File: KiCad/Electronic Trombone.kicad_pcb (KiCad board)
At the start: 2 copper layers, 167 parts, among them J1 691137710004, J2 691137710003, J3 691137710003, J4 691137710002, Q1 NPN, Q2 PNP, Q3 NPN, Q4 PNP, Q5 NPN, Q6 NPN, SW1 SW_Push_Dual, SW2 SW_Push_Dual, SW3 SW_Push_Dual, SW4 SW_DPST, U1 CD74HC4051E, U10 TL074, U2 TL074, U3 TL074, U4 40106, U5 TL074, U6 TL074, U7 TL074, U8 TL074, U9 TL074

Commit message: started pcb layout
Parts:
- moved R17 217.5 mm to (-79.6, 83.8)
- moved C20 213.4 mm to (-189.7, 101.9)
- moved C21 213.4 mm to (-189.7, 103.6)
- moved C22 213.4 mm to (-189.7, 105.4)
- moved C23 213.4 mm to (-189.7, 107.1)
- moved C24 213.4 mm to (-189.7, 108.9)
- moved C25 213.4 mm to (-189.7, 110.6)
- moved C26 213.4 mm to (-189.7, 112.4)
- moved C27 213.4 mm to (-189.7, 114.1)
- moved C5 213.4 mm to (-180.4, 139.6)
- moved C6 213.4 mm to (-180.4, 146.2)
- moved C7 213.4 mm to (-180.4, 152.7)
- moved J4 213.4 mm to (-177.8, 105.3)
- moved R18 213.4 mm to (-73.3, 69.8)
- moved R20 213.4 mm to (-73.3, 71.6)
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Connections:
- net Net-(D1-K) renamed //Oscillator/Sch Inv In 1
- net Net-(D2-K) renamed //Oscillator/Sch Inv In 2
- net Net-(R17-Pad1) renamed //Oscillator/Tuning 1
- net Net-(R26-Pad1) renamed //Oscillator/Tuning 2
- net Net-(U1-S0) renamed //Trigger 1
- net Net-(U1-S1) renamed //Trigger 2
- net Net-(U1-S2) renamed //Trigger 3
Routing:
- net GND: track 0.00 -> 21.0 mm
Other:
- board outline added: 150 x 100 mm

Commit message: added osc core and tuning to pcb layout
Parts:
- R19, R28: value 2.5k -> 2.4k; footprint Resistor_SMD:R_0603_1608Metric -> Resistor_SMD:R_0201_0603Metric
- moved SW1 259.3 mm to (69.2, 113.5)
- moved J4 249.6 mm to (71.8, 103.0)
- moved SW2 247.3 mm to (69.2, 127.2)
- moved SW4 237.7 mm to (123.0, 82.5), turned to 90 degrees
- moved SW3 236.0 mm to (69.0, 141.0)
- moved TH4 199.6 mm to (101.9, 78.5), turned to 180 degrees
- moved TH6 199.3 mm to (101.9, 70.0), turned to 180 degrees
- moved TH5 199.2 mm to (101.9, 61.5), turned to 180 degrees
- moved RV10 193.2 mm to (130.0, 53.1), turned to 180 degrees
- moved R27 176.1 mm to (105.0, 83.2)
- moved R22 175.2 mm to (101.6, 84.1)
- moved R24 175.1 mm to (101.6, 85.0), turned to 180 degrees
- moved R23 175.1 mm to (101.6, 83.2)
- moved J3 166.7 mm to (54.5, 107.0), turned to -90 degrees
- moved R26 165.6 mm to (94.1, 56.7)
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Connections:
- J1 pad 1: //Pot Out -> //Audio Out
- J1 pad 2: //Audio Out -> //Pot Out
- R20 pad 2: Net-(U5C-+) -> Net-(U5D-+)
- R21 pad 2: Net-(U5C-+) -> Net-(U5D-+)
- SW4 pad 1: Net-(B2-Pad2) -> Net-(B1-Pad1)
- SW4 pad 2: -9V -> +9V
- SW4 pad 3: Net-(B1-Pad1) -> Net-(B2-Pad2)
- SW4 pad 4: +9V -> -9V
- U5 pad 1: //Oscillator/Mix In 1 -> //Oscillator/Mix In 2
- U5 pad 10: Net-(U5C-+) -> GND
- U5 pad 12: GND -> Net-(U5D-+)
- U5 pad 13: Net-(U5D--) -> //Filter/Signal In
- U5 pad 14: Net-(U5D--) -> //Filter/Signal In
- U5 pad 2: //Oscillator/Mix In 1 -> //Oscillator/Mix In 2
- U5 pad 3: //Oscillator/Sch Inv In 1 -> //Oscillator/Sch Inv In 2
- U5 pad 5: //Oscillator/Sch Inv In 2 -> //Oscillator/Sch Inv In 1
- U5 pad 6: //Oscillator/Mix In 2 -> //Oscillator/Mix In 1
- U5 pad 7: //Oscillator/Mix In 2 -> //Oscillator/Mix In 1
- U5 pad 8: //Filter/Signal In -> Net-(U5C--)
- U5 pad 9: //Filter/Signal In -> Net-(U5C--)
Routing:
- net GND: track 21.0 -> 0.00 mm
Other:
- board text added: "-Control Buttons Board Below-"
- board text added: "-Pot Terminals Control Board Below-"
- board text added: "Tr. 1"
- board text added: "Tr. 2"
- board text added: "Tr. 3"

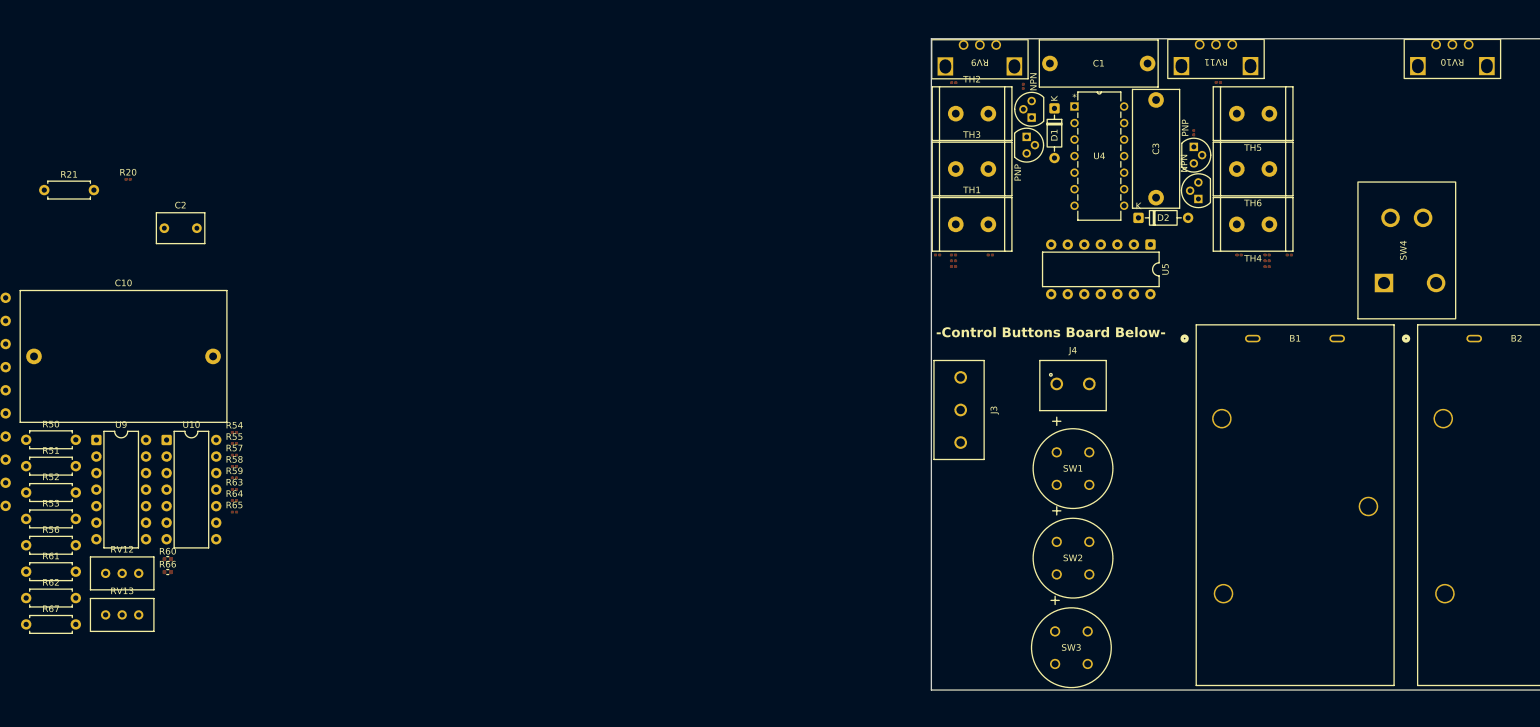
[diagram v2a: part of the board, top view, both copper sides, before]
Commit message: added osc output processing to pcb layout
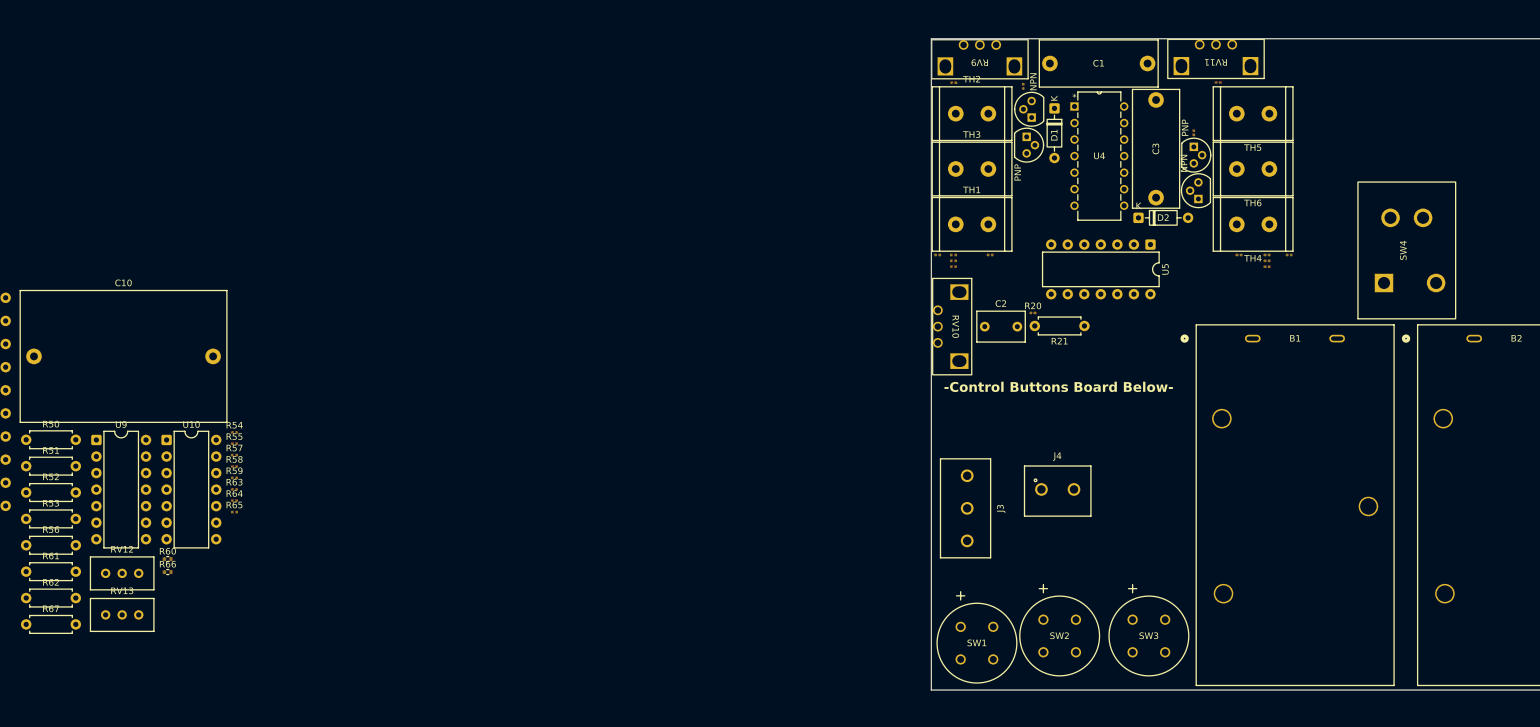
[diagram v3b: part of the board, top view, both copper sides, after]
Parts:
- moved R21 161.1 mm to (73.5, 94.1), turned to 180 degrees
- moved R20 140.4 mm to (65.6, 92.1)
- moved C2 126.9 mm to (58.2, 94.2)
- moved RV10 87.1 mm to (53.2, 94.2), turned to -90 degrees
- moved SW1 30.6 mm to (54.5, 140.3)
- moved J4 16.4 mm to (69.4, 119.2)
- moved J3 15.1 mm to (55.5, 122.1)
- moved SW2 12.1 mm to (67.2, 139.2)
- moved SW3 12.0 mm to (80.9, 139.2)
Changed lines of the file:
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@@
 	(footprint "Resistor_SMD:R_0201_0603Metric"
 		(layer "F.Cu")
-		(at -73.325 71.585)
+		(at 65.6 92.1)
 		(descr "Resistor SMD 0201 (0603 Metric), square (rectangular) end terminal, IPC-7351 nominal, (Body size source: https://www.vishay.com/docs/20052/crcw0201e3.pdf)")
 		(tags "resistor")
@@
 	(footprint "Header 691137710002:691137710002"
 		(layer "F.Cu")
-		(at 71.75 103)
+		(at 69.4 119.2)
 		(property "Reference" "J4"
 			(at 0 -5.135 0)
@@
 	(footprint "Switch Push Button D6R90F2LFS:D6R90_CNK"
 		(layer "F.Cu")
-		(at 69.25 127.25)
+		(at 67.2 139.2)
 		(tags "D6R90F2LFS ")
 		(property "Reference" "SW2"
@@
 	(footprint "Resistor_THT:R_Axial_DIN0207_L6.3mm_D2.5mm_P7.62mm_Horizontal"
 		(layer "F.Cu")
-		(at -86.205 73.235)
+		(at 73.5 94.1 180)
 		(descr "Resistor, Axial_DIN0207 series, Axial, Horizontal, pin pitch=7.62mm, 0.25W = 1/4W, length*diameter=6.3*2.5mm^2, http://cdn-reichelt.de/documents/datenblatt/B400/1_4W%23YAG.pdf")
 		(tags "Resistor Axial_DIN0207 series Axial Horizontal pin pitch 7.62mm 0.25W = 1/4W length 6.3mm diameter 2.5mm")
@@
 		(duplicate_pad_numbers_are_jumpers no)
 		(fp_line
-			(start 0.54 -1.37)
-			(end 7.08 -1.37)
+			(start 7.08 1.37)
+			(end 7.08 1.04)
 			(stroke
 				(width 0.12)
@@
 		)
 		(fp_line
-			(start 0.54 -1.04)
-			(end 0.54 -1.37)
+			(start 7.08 -1.37)
+			(end 7.08 -1.04)
 			(stroke
 				(width 0.12)
@@
 		)
 		(fp_line
-			(start 0.54 1.04)
-			(end 0.54 1.37)
+			(start 0.54 1.37)
+			(end 7.08 1.37)
 			(stroke
 				(width 0.12)
@@
 		)
 		(fp_line
-			(start 0.54 1.37)
-			(end 7.08 1.37)
+			(start 0.54 1.04)
+			(end 0.54 1.37)
 			(stroke
 				(width 0.12)
@@
 		)
 		(fp_line
-			(start 7.08 -1.37)
-			(end 7.08 -1.04)
+			(start 0.54 -1.04)
+			(end 0.54 -1.37)
 			(stroke
 				(width 0.12)
@@
 		)
 		(fp_line
-			(start 7.08 1.37)
-			(end 7.08 1.04)
+			(start 0.54 -1.37)
+			(end 7.08 -1.37)
 			(stroke
 				(width 0.12)
@@
 		)
 		(fp_line
-			(start 0 0)
-			(end 0.66 0)
+			(start 7.62 0)
+			(end 6.96 0)
 			(stroke
 				(width 0.1)
@@
 		)
 		(fp_line
-			(start 7.62 0)
-			(end 6.96 0)
+			(start 0 0)
+			(end 0.66 0)
 			(stroke
 				(width 0.1)
@@
 		)
 		(pad "1" thru_hole circle
-			(at 0 0)
+			(at 0 0 180)
 			(size 1.6 1.6)
 			(drill 0.8)
@@
 		)
 		(pad "2" thru_hole circle
-			(at 7.62 0)
+			(at 7.62 0 180)
 			(size 1.6 1.6)
 			(drill 0.8)
@@
 	(footprint "Capacitor_THT:C_Rect_L7.2mm_W4.5mm_P5.00mm"
 		(layer "F.Cu")
-		(at -67.775 79.085)
+		(at 58.2 94.2)
 		(descr "C, Rect series, Radial, pin pitch=5.00mm, length*width=7.2*4.5mm^2, Capacitor, R82, https://content.kemet.com/datasheets/KEM_F3101_R82.pdf")
 		(tags "C Rect series Radial pin pitch 5.00mm length 7.2mm width 4.5mm Capacitor R82")
@@
 	(footprint "Switch Push Button D6R90F2LFS:D6R90_CNK"
 		(layer "F.Cu")
-		(at 69.25 113.5)
+		(at 54.5 140.30001)
 		(tags "D6R90F2LFS ")
 		(property "Reference" "SW1"
@@
 	(footprint "Potentiometer 100k PTV09A-2020F-B104:Potentiometer 100k PTV09A-2020F-B104"
 		(layer "F.Cu")
-		(at 130 53.1 180)
+		(at 53.2 94.2 -90)
 		(property "Reference" "RV10"
-			(at 0 -0.5 180)
+			(at 0 -0.5 270)
 			(unlocked yes)
 			(layer "F.SilkS")
@@
 		)
 		(property "Value" "100k"
-			(at 0 1 180)
+			(at 0 1 270)
 			(unlocked yes)
 			(layer "F.Fab")
@@
 		)
 		(property "Datasheet" ""
-			(at 0 0 180)
+			(at 0 0 270)
 			(unlocked yes)
 			(layer "F.Fab")
@@
 		)
 		(property "Description" "Potentiometer, US symbol"
-			(at 0 0 180)
+			(at 0 0 270)
 			(unlocked yes)
 			(layer "F.Fab")
@@
 		)
 		(property "Sim.Device" "R"
-			(at 0 0 180)
+			(at 0 0 270)
 			(unlocked yes)
 			(layer "F.Fab")
@@
 		)
 		(property "Sim.Type" "POT"
-			(at 0 0 180)
+			(at 0 0 270)
 			(unlocked yes)
 			(layer "F.Fab")
@@
 		)
 		(property "Sim.Pins" "1=r0 2=wiper 3=r1"
-			(at 0 0 180)
+			(at 0 0 270)
 			(unlocked yes)
 			(layer "F.Fab")
@@
 		)
 		(fp_text user "${REFERENCE}"
-			(at 0 2.5 180)
+			(at 0 2.5 270)
 			(unlocked yes)
 			(layer "F.Fab")
@@
 		)
 		(pad "" np_thru_hole rect
-			(at -5.3 -1.1 180)
+			(at -5.3 -1.1 270)
 			(size 2.4 2.8)
 			(drill oval 1.8 2.2)
@@
 		)
 		(pad "" np_thru_hole rect
-			(at 5.3 -1.1 180)
+			(at 5.3 -1.1 270)
 			(size 2.4 2.8)
 			(drill oval 1.8 2.2)
@@
 		)
 		(pad "1" thru_hole circle
-			(at -2.5 2.2 180)
+			(at -2.5 2.2 270)
 			(size 1.5 1.5)
 			(drill 1)
@@
 		)
 		(pad "2" thru_hole circle
-			(at 0 2.2 180)
+			(at 0 2.2 270)
 			(size 1.5 1.5)
 			(drill 1)
@@
 		)
 		(pad "3" thru_hole circle
-			(at 2.5 2.2 180)
+			(at 2.5 2.2 270)
 			(size 1.5 1.5)
 			(drill 1)
@@
 	(footprint "Header 691137710003:691137710003"
 		(layer "F.Cu")
-		(at 54.5 107 -90)
+		(at 55.5 122.1 -90)
 		(property "Reference" "J3"
 			(at 0 -5.135 90)
@@
 	(footprint "Switch Push Button D6R90F2LFS:D6R90_CNK"
 		(layer "F.Cu")
-		(at 69 141)
+		(at 80.9 139.2)
 		(tags "D6R90F2LFS ")
 		(property "Reference" "SW3"
@@
 	)
 	(gr_text "-Control Buttons Board Below-"
-		(at 50.7 96 0)
+		(at 51.9 104.4 0)
 		(layer "F.SilkS")
 		(effects

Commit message: minor but important changes to schematic
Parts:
- added C30: 0.1u, Capacitor_SMD:C_0201_0603Metric, F.Cu at (216.2, 100.8)
- added C31: 0.1u, Capacitor_SMD:C_0201_0603Metric, F.Cu at (216.2, 102.5)
- added R75: R_US, Resistor_THT:R_Axial_DIN0207_L6.3mm_D2.5mm_P7.62mm_Horizontal, F.Cu at (188.6, 115.5)
- added R76: R_US, Resistor_THT:R_Axial_DIN0207_L6.3mm_D2.5mm_P7.62mm_Horizontal, F.Cu at (188.6, 119.6)
- added U11: TL074, Package_DIP:DIP-14_W7.62mm, F.Cu at (158.5, 124.9)
- moved R1 370.8 mm to (183.2, 119.9)
- moved R2 370.8 mm to (183.2, 121.6)
- moved R3 370.8 mm to (183.2, 123.4)
- moved R4 370.8 mm to (183.2, 125.1)
- moved R72 357.6 mm to (172.8, 114.5), turned to 180 degrees
- moved R74 357.6 mm to (172.8, 115.6)
- moved R71 355.2 mm to (170.2, 115.7)
- moved R73 355.1 mm to (170.2, 114.6), turned to 180 degrees
- moved U1 310.3 mm to (185.5, 148.7)
- moved U2 57.5 mm to (-93.4, 94.9)
- moved C9 52.3 mm to (-107.3, 184.3)
- moved R61 52.3 mm to (-96.8, 183.6)
- moved R66 52.3 mm to (-75.1, 183.6)
- moved D11 52.3 mm to (-107.6, 145.1)
- moved D13 52.3 mm to (-107.6, 152.2)
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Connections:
- net Net-(U3D--) renamed /Power/Thaw 3
- net Net-(U5C--) renamed /Power/Thaw 5
- net Net-(U7D--) renamed /Power/Thaw 7
- net Net-(U8D--) renamed /Power/Thaw 8
- R1 pad 2: Net-(U2B-+) -> Net-(U11B-+)
- R2 pad 1: Net-(U2B-+) -> Net-(U11B-+)
- R3 pad 2: Net-(U2B--) -> Net-(U11B--)
- R4 pad 1: Net-(U2B--) -> Net-(U11B--)
- R5 pad 1: Net-(U2C--) -> Net-(U2B--)
- R6 pad 2: Net-(U2C--) -> Net-(U2B--)
- R71 pad 1: -5V -> Net-(U11D-+)
- R72 pad 1: +5V -> Net-(U11A-+)
- R73 pad 2: -5V -> Net-(U11D-+)
- R74 pad 2: +5V -> Net-(U11A-+)
- RV8 pad 2: Net-(U2D-+) -> Net-(U2C-+)
- U2 pad 10: //Amplifier/Out -> Net-(U2C-+)
- U2 pad 12: Net-(U2D-+) -> GND
- U2 pad 13: //Audio Out -> /Power/Thaw 2
- U2 pad 14: //Audio Out -> /Power/Thaw 2
- U2 pad 5: Net-(U2B-+) -> //Amplifier/Out
- U2 pad 7: //-Pot -> Net-(R5-Pad2)
- U2 pad 8: Net-(R5-Pad2) -> //Audio Out
- U2 pad 9: Net-(U2C--) -> //Audio Out
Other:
- board text added: "1"
- board text added: "2"
- board text added: "3"
- board text removed: "Tr. 1"
- board text removed: "Tr. 2"
- board text removed: "Tr. 3"

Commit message: fixed custom pot voltage control schematic
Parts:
- removed R75, R76: R_US, Resistor_THT:R_Axial_DIN0207_L6.3mm_D2.5mm_P7.62mm_Horizontal
- added J5: 691137710002, Header 691137710002:691137710002, F.Cu at (195.5, 144.4)
- added RV14: 20k, Potentiometer_SMD:Potentiometer_Bourns_TC33X_Vertical, F.Cu at (214.4, 121.9)
- J1: value 691137710004 -> 691137710002; footprint Header 691137710004:691137710004 -> Header 691137710002:691137710002
- moved RV1 294.1 mm to (160.6, 111.6)
- moved RV2 294.1 mm to (160.6, 116.3)
- moved RV3 294.1 mm to (160.6, 121.1)
- moved RV4 294.1 mm to (160.6, 125.8)
- moved RV5 294.1 mm to (160.6, 130.6)
- moved RV6 294.1 mm to (160.6, 135.3)
- moved RV7 294.1 mm to (160.6, 140.1)
- moved U5 46.5 mm to (38.6, 92.9)
- moved R73 28.6 mm to (188.0, 137.0)
- moved R71 28.6 mm to (188.0, 138.1)
- moved R72 22.8 mm to (176.6, 137.0)
- moved R74 22.8 mm to (176.6, 138.1)
- moved U11 21.4 mm to (178.5, 132.5)
- moved U1 21.3 mm to (186.0, 127.4)
- moved R1 17.8 mm to (169.4, 131.2)
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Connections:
- net //+Pot 1st Partial renamed /Custom Potentiometer Controls/+Pot 1st Partial
- net //+Pot 6th Partial renamed /Custom Potentiometer Controls/+Pot 6th Partial
- net //+Pot 7th Partial renamed /Custom Potentiometer Controls/+Pot 7th Partial
- net //Trigger 1 renamed /Custom Potentiometer Controls/Trigger 1
- net //Trigger 2 renamed /Custom Potentiometer Controls/Trigger 2
- net //Trigger 3 renamed /Custom Potentiometer Controls/Trigger 3
- C10 pad 1: //In -> //Audio Control
- C8 pad 1: //In -> //Audio Control
- J1 pad 2: //Pot Out -> //Audio Control
- R1 pad 1: //-Pot -> /Custom Potentiometer Controls/Pot Voltage Difference
- R1 pad 2: Net-(U11B-+) -> Net-(U11C--)
- R2 pad 1: Net-(U11B-+) -> /Custom Potentiometer Controls/Mux Out
- R2 pad 2: //+Pot -> Net-(U11C-+)
- R3 pad 1: GND -> Net-(U11C--)
- R3 pad 2: Net-(U11B--) -> /Custom Potentiometer Controls/-Pot
- R4 pad 1: Net-(U11B--) -> GND
- R4 pad 2: //Pot Voltage Difference -> Net-(U11C-+)
- RV2 pad 2: //+Pot 4th Partial -> /Custom Potentiometer Controls/+Pot 2nd Partial
- RV3 pad 2: //+Pot 2nd Partial -> /Custom Potentiometer Controls/+Pot 3rd Partial
- RV4 pad 2: //+Pot 5th Partial -> /Custom Potentiometer Controls/+Pot 4th Partial
- RV5 pad 2: //+Pot 3rd Partial -> /Custom Potentiometer Controls/+Pot 5th Partial
- U1 pad 1: //+Pot 4th Partial -> /Custom Potentiometer Controls/+Pot 4th Partial
- U1 pad 12: //+Pot 3rd Partial -> /Custom Potentiometer Controls/+Pot 3rd Partial
- U1 pad 15: //+Pot 2nd Partial -> /Custom Potentiometer Controls/+Pot 2nd Partial
- U1 pad 3: //+Pot -> /Custom Potentiometer Controls/Mux Out
- U1 pad 5: //+Pot 5th Partial -> /Custom Potentiometer Controls/+Pot 5th Partial
- U11 pad 10: GND -> Net-(U11C-+)
- U11 pad 5: Net-(U11B-+) -> /Custom Potentiometer Controls/Mux Out
- U11 pad 6: Net-(U11B--) -> /Custom Potentiometer Controls/+Pot
- U11 pad 7: //-Pot -> /Custom Potentiometer Controls/+Pot
- U11 pad 8: /Power/Thaw 11 -> /Custom Potentiometer Controls/-Pot
- U11 pad 9: /Power/Thaw 11 -> Net-(U11C--)
- U2 pad 3: //Pot Out -> //Audio Control
- U9 pad 10: //In -> //Audio Control
- U9 pad 5: //In -> //Audio Control
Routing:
- net Net-(U11D-+): track 0.00 -> 3.11 mm
- net Net-(U11A-+): track 0.00 -> 2.62 mm
- net -5V: track 0.00 -> 2.54 mm
- net +5V: track 0.00 -> 2.54 mm
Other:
- board text added: "+"
- board text added: "-"
- board text added: "Mux"

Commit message: placed and routed custom pot control
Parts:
- added C32: 0.1u, Capacitor_SMD:C_0201_0603Metric, F.Cu at (184.1, 109.1)
- added C33: 0.1u, Capacitor_SMD:C_0201_0603Metric, F.Cu at (173.0, 124.4)
- moved R68 228.2 mm to (41.7, 129.9)
- moved R69 228.2 mm to (41.7, 131.7)
- moved R70 228.2 mm to (41.7, 133.4)
- moved C30 58.1 mm to (173.0, 139.6), turned to 180 degrees
- moved C31 48.9 mm to (184.2, 139.6), turned to 180 degrees
- moved RV14 36.7 mm to (186.9, 146.2), turned to 90 degrees
- moved RV2 28.1 mm to (187.9, 109.9), turned to 180 degrees
- moved RV1 27.7 mm to (187.9, 116.1), turned to 180 degrees
- moved RV3 27.3 mm to (187.9, 122.3), turned to 180 degrees
- moved RV6 21.0 mm to (168.8, 116.0)
- moved RV7 19.7 mm to (168.8, 122.2)
- moved R1 19.6 mm to (184.3, 144.0), turned to 180 degrees
- moved R3 18.6 mm to (184.3, 146.0), turned to 180 degrees
- moved RV4 18.0 mm to (168.8, 109.8)
- moved R71 15.1 mm to (172.9, 136.6), turned to 180 degrees
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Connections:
- J2 pad 1: /Custom Potentiometer Controls/Trigger 1 -> /Custom Potentiometer Controls/Trigger 3
- J2 pad 3: /Custom Potentiometer Controls/Trigger 3 -> /Custom Potentiometer Controls/Trigger 1
- R2 pad 1: /Custom Potentiometer Controls/Mux Out -> /Custom Potentiometer Controls/+Pot
- R71 pad 1: Net-(U11D-+) -> Net-(U11A-+)
- R72 pad 1: Net-(U11A-+) -> Net-(U11D-+)
- R73 pad 2: Net-(U11D-+) -> Net-(U11A-+)
- R74 pad 2: Net-(U11A-+) -> Net-(U11D-+)
- U11 pad 1: +5V -> -5V
- U11 pad 13: -5V -> +5V
- U11 pad 14: -5V -> +5V
- U11 pad 2: +5V -> -5V
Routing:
- net /Custom Potentiometer Controls/Mux Out: track 0.00 -> 30.9 mm
- net /Custom Potentiometer Controls/+Pot: track 0.00 -> 28.4 mm
- net +5V: track 2.54 -> 28.8 mm
- net /Custom Potentiometer Controls/-Pot: track 0.00 -> 17.3 mm
- net /Custom Potentiometer Controls/Trigger 3: track 0.00 -> 17.0 mm
- net /Custom Potentiometer Controls/Trigger 2: track 0.00 -> 16.0 mm
- net /Custom Potentiometer Controls/Trigger 1: track 0.00 -> 15.0 mm
- net /Custom Potentiometer Controls/+Pot 5th Partial: track 0.00 -> 10.9 mm
- net Net-(U11C-+): track 0.00 -> 10.7 mm
- net -5V: track 2.54 -> 13.2 mm
- net /Custom Potentiometer Controls/+Pot 7th Partial: track 0.00 -> 7.23 mm
- net /Custom Potentiometer Controls/+Pot 6th Partial: track 0.00 -> 6.16 mm
- net /Custom Potentiometer Controls/+Pot 3rd Partial: track 0.00 -> 5.41 mm
- net /Custom Potentiometer Controls/+Pot 1st Partial: track 0.00 -> 4.92 mm
- net /Custom Potentiometer Controls/+Pot 2nd Partial: track 0.00 -> 4.90 mm
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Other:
- board text added: "Adj Cust Pot Diff"
- board text added: "Pot Terminals Controller"
- board text removed: "-Pot Terminals Control Board Below-"
